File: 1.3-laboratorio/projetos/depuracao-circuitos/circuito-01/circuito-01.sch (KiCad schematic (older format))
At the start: 20 parts, among them J1 Conn_01x07_Male, J2 Conn_01x07_Male, J3 Conn_01x07_Male, J4 Conn_01x07_Male, J5 Conn_01x07_Male, J6 Conn_01x07_Male, P1 CONN_01X02, SW1 SW_DIP_x04, U1 74LS32, U2 7400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

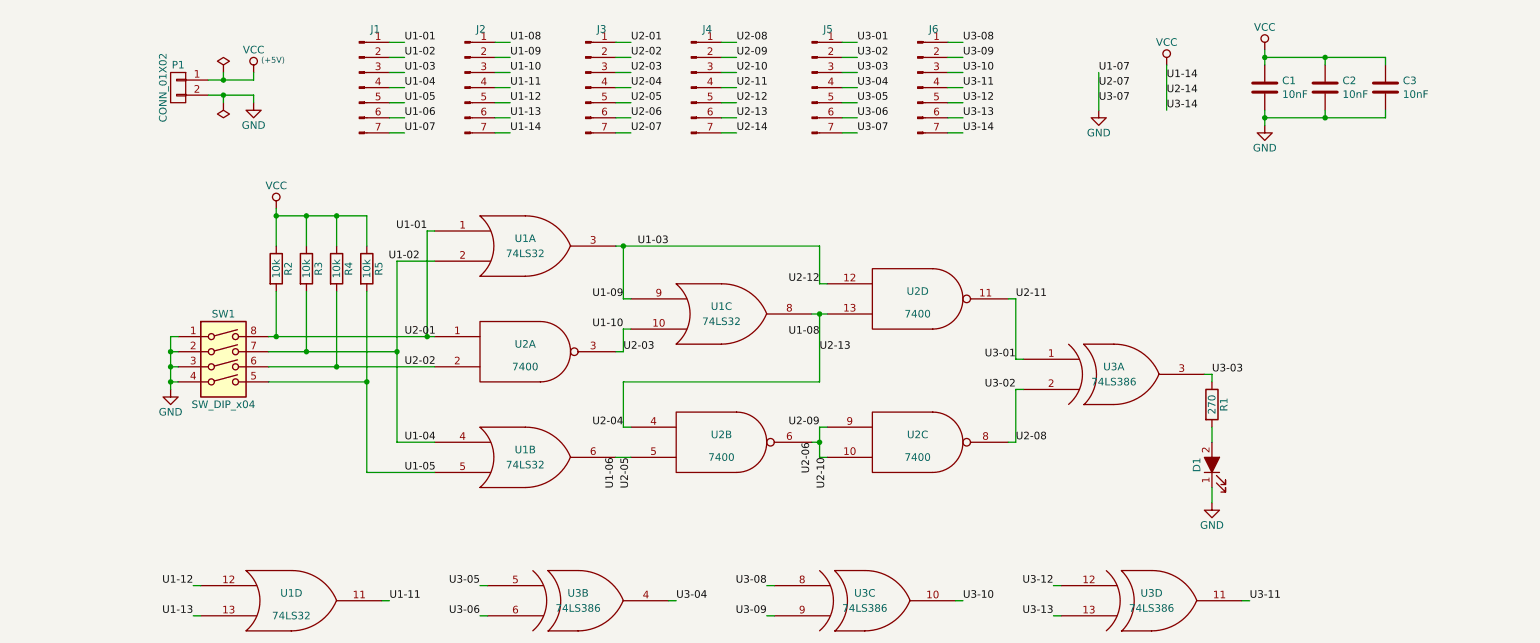
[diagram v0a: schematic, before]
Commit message: Leiaute promissor para Circuito 01.
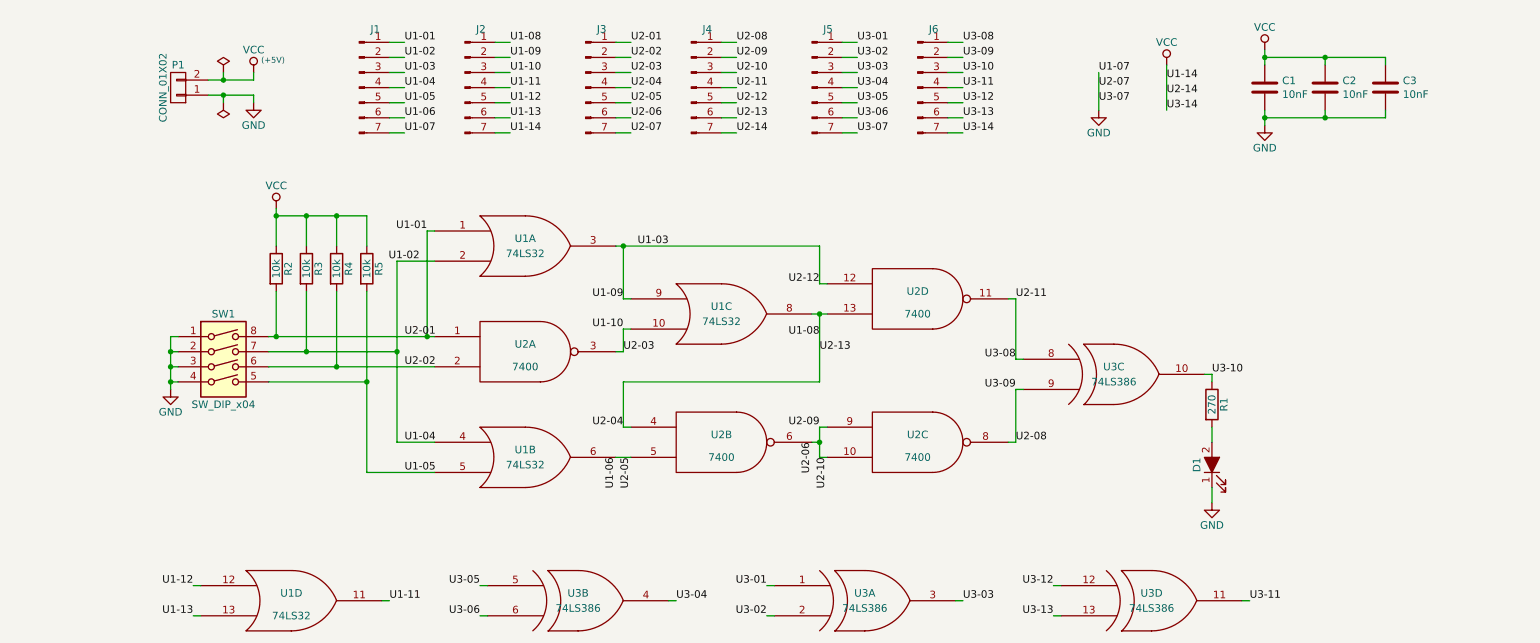
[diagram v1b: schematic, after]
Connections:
- net GND: now also P1.1 (P1); no longer P1.2 (P2)
- net U2-08: now also J6.2 (Pin_2), U3.9; no longer J5.2 (Pin_2), U3.2
- net U2-11: now also J6.1 (Pin_1), U3.8; no longer J5.1 (Pin_1), U3.1
- net U3-03: now also U3.3; no longer R1.1, U3.3
- net U3-10: now also R1.1, U3.10; no longer U3.10
- net VCC: now also P1.2 (P2); no longer P1.1 (P1)
- removed net U3-08: J6.1 (Pin_1), U3.8
- removed net U3-09: J6.2 (Pin_2), U3.9
- new net U3-01: J5.1 (Pin_1), U3.1
- new net U3-02: J5.2 (Pin_2), U3.2
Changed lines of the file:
@@
 $Comp
 L circuito-01-rescue:74LS386 U3
-U 1 1 5B0DB8C7
+U 3 1 5B0DB8C7
 P 8450 3850
 F 0 "U3" H 8450 3900 50  0000 C CNN
@@
 F 2 "Package_DIP:DIP-14_W7.62mm_Socket_LongPads" H 8450 3850 50  0001 C CNN
 F 3 "" H 8450 3850 50  0001 C CNN
-	1    8450 3850
+	3    8450 3850
 	1    0    0    -1
 $EndComp
@@
 U 1 1 5B189AF0
 P 2250 1950
-F 0 "P1" H 2250 2100 50  0000 C CNN
+F 0 "P1" H 2250 1800 50  0000 C CNN
 F 1 "CONN_01X02" V 2350 1950 50  0000 C CNN
 F 2 "TerminalBlock_Altech:Altech_AK300_1x02_P5.00mm_45-Degree" H 2250 1950 50  0001 C CNN
 F 3 "" H 2250 1950 50  0000 C CNN
 	1    2250 1950
-	-1   0    0    -1
+	-1   0    0    1
 $EndComp
 $Comp
@@
 U2-08
 Text Label 7800 3950 2    50   ~ 0
-U3-02
+U3-09
 Text Label 7800 3750 2    50   ~ 0
-U3-01
+U3-08
 Text Label 9100 3850 0    50   ~ 0
-U3-03
+U3-10
 $Comp
 L circuito-01-rescue:GND #PWR0101
@@
 $Comp
 L circuito-01-rescue:74LS386 U3
-U 3 1 5CCB67AB
+U 1 1 5CCB67AB
 P 6800 5350
 F 0 "U3" H 6800 5400 50  0000 C CNN
@@
 F 2 "Package_DIP:DIP-14_W7.62mm_Socket_LongPads" H 6800 5350 50  0001 C CNN
 F 3 "" H 6800 5350 50  0001 C CNN
-	3    6800 5350
+	1    6800 5350
 	1    0    0    -1
 $EndComp
@@
 U3-06
 Text Label 6150 5250 2    50   ~ 0
-U3-08
+U3-01
 Text Label 6150 5450 2    50   ~ 0
-U3-09
+U3-02
 Text Label 8050 5250 2    50   ~ 0
 U3-12
@@
 U3-11
 Text Label 7450 5350 0    50   ~ 0
-U3-10
+U3-03
 Text Label 5550 5350 0    50   ~ 0
 U3-04

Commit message: Leiaute em elaboração para o Circuito 01.
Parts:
- added J7, J8: Conn_01x04, Connector_PinSocket_2.54mm:PinSocket_1x04_P2.54mm_Vertical, symbol Connector_Generic:Conn_01x04
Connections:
- net U1-01: now also J7.1 (Pin_1), J8.1 (Pin_1)
- net U1-02: now also R4.2; no longer R3.2
- net U1-06: now also J7.3 (Pin_3), J8.3 (Pin_3)
- net U2-02: now also R3.2, J7.2 (Pin_2), J8.2 (Pin_2); no longer R4.2
- net U3-10: now also J7.4 (Pin_4), J8.4 (Pin_4)
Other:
- moved on the sheet: C1, C2, C3, J1, J2, J3, J4, J5, J6

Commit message: Leiaute quase finalizado para Circuito 01.
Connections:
- net U1-02: now also J7.2 (Pin_2), J8.2 (Pin_2)
- net U1-06: no longer J7.3 (Pin_3), J8.3 (Pin_3)
- net U2-02: now also J7.3 (Pin_3), J8.3 (Pin_3); no longer J7.2 (Pin_2), J8.2 (Pin_2)
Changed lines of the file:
@@
 Text Label 10300 1550 2    50   ~ 0
 U1-01
-Text Label 10300 1650 2    50   ~ 0
+Text Label 10300 1750 2    50   ~ 0
 U2-02
-Text Label 10300 1750 2    50   ~ 0
-U1-06
 Text Label 10300 2050 2    50   ~ 0
 U1-01
-Text Label 10300 2150 2    50   ~ 0
+Text Label 10300 2250 2    50   ~ 0
 U2-02
-Text Label 10300 2250 2    50   ~ 0
-U1-06
 Text Label 10300 1850 2    50   ~ 0
 U3-10
 Text Label 10300 2350 2    50   ~ 0
 U3-10
+Text Label 10300 1650 2    50   ~ 0
+U1-02
+Text Label 10300 2150 2    50   ~ 0
+U1-02
 $EndSCHEMATC

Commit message: Concluído o leiaute de Circuito 01.
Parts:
- J7, J8: value Conn_01x04 -> Conn_01x05; footprint Connector_PinSocket_2.54mm:PinSocket_1x04_P2.54mm_Vertical -> Connector_PinSocket_2.54mm:PinSocket_1x05_P2.54mm_Vertical; symbol Connector_Generic:Conn_01x04 -> Connector_Generic:Conn_01x05
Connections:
- net GND: now also J7.5 (Pin_5)
- no-connect marks 0 -> 1
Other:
- moved on the sheet: C1, C2, C3, D1, J1, J2, J3, J4, J5, J6, P1, R1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
